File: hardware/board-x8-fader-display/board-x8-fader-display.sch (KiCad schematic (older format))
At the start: 10 parts

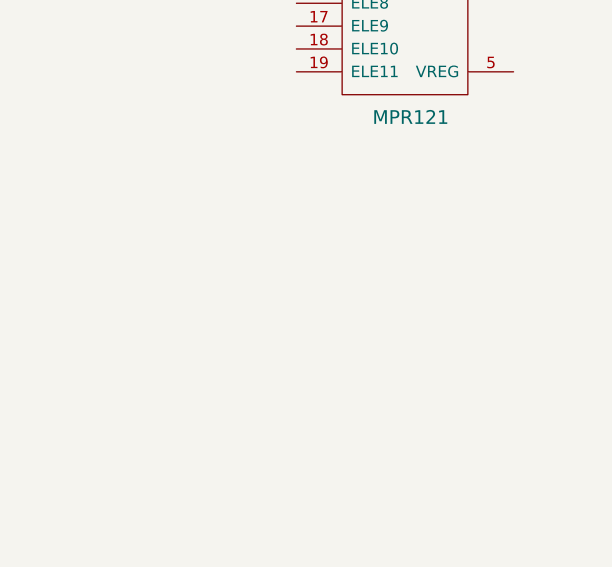
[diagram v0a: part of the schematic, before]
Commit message: Adding L293 lib, moving motor to sensible place in fader lib
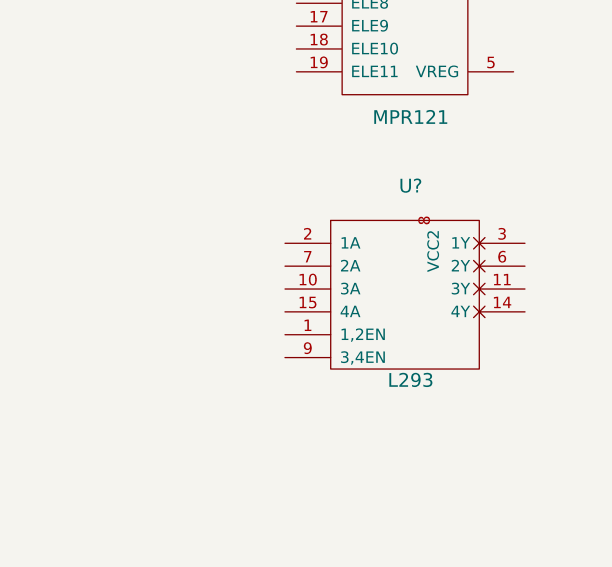
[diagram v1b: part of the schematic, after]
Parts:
- added U?: L293, symbol L293
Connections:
- net GND: now also U?.12 (GND), U?.13 (GND), U?.4 (GND), U?.5 (GND)
- net VCC: now also U?.16 (VCC)
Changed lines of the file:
@@
 LIBS:contrib
 LIBS:valves
+LIBS:board-x8-fader-display-cache
 EELAYER 25 0
 EELAYER END
@@
 	1    0    0    -1
 $EndComp
+$Comp
+L L293 U?
+U 1 1 5A6CD376
+P 3450 4950
+F 0 "U?" H 3450 5400 60  0000 C CNN
+F 1 "L293" H 3450 4550 60  0000 C CNN
+F 2 "" H 3400 4650 60  0001 C CNN
+F 3 "" H 3400 4650 60  0001 C CNN
+	1    3450 4950
+	1    0    0    -1
+$EndComp

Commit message: Fader board schematic updates
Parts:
- removed U?: L293, symbol L293
- added U?: L293, symbol L293
- added U?: 74xx238, symbol 74xx238
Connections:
- net GND: now also U?.12 (GND), U?.13 (GND), U?.4 (GND), U?.5 (GND), U?.8 (GND)
- net VCC: now also U?.16 (VCC), U?.16 (VCC)
- net at RV?.1: now also RV?.1, RV?.1, RV?.1, RV?.1, RV?.1, RV?.1, RV?.1
- net X0: now reaches RV?.2
- net X0: now also U?.13 (X0)
- net at RV?.3: now also RV?.3, RV?.3, RV?.3, RV?.3, RV?.3, RV?.3, RV?.3
- net at RV?.A: now also U?.3 (1Y)
- net at RV?.B: now also U?.6 (2Y)
- net ELE0: now reaches RV?.T (Touch)
- net ELE0: now also U?.8 (ELE0)
- net X1: now reaches RV?.2
- net X1: now also U?.14 (X1)
- net at RV?.A: now also U?.11 (3Y)
- net at RV?.B: now also U?.14 (4Y)
- net ELE1: now reaches RV?.T (Touch)
- net ELE1: now also U?.9 (ELE1)
- net X2: now reaches RV?.2
- net X2: now also U?.15 (X2)
- net ELE2: now reaches RV?.T (Touch)
- net ELE2: now also U?.10 (ELE2)
- net X3: now reaches RV?.2
- net X3: now also U?.12 (X3)
- net ELE3: now reaches RV?.T (Touch)
- net ELE3: now also U?.11 (ELE3)
- net X4: now reaches RV?.2
- net X4: now also U?.1 (X4)
- net ELE4: now reaches RV?.T (Touch)
- net ELE4: now also U?.12 (ELE4)
- net X5: now reaches RV?.2
- net X5: now also U?.5 (X5)
- net ELE5: now reaches RV?.T (Touch)
- net ELE5: now also U?.13 (ELE5)
- net X6: now reaches RV?.2
- net X6: now also U?.2 (X6)
- net ELE6: now reaches RV?.T (Touch)
- net ELE6: now also U?.14 (ELE6)
- net X7: now reaches RV?.2
- net X7: now also U?.4 (X7)
- net ELE7: now reaches RV?.T (Touch)
- net ELE7: now also U?.15 (ELE7)
- new net: U?.1 (1,2EN), U?.15 (Y0)
- new net: U?.10 (3A), U?.2 (1A)
- new net: U?.15 (4A), U?.7 (2A)
- new net: U?.14 (Y1), U?.9 (3,4EN)
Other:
- moved on the sheet: RV?, U?

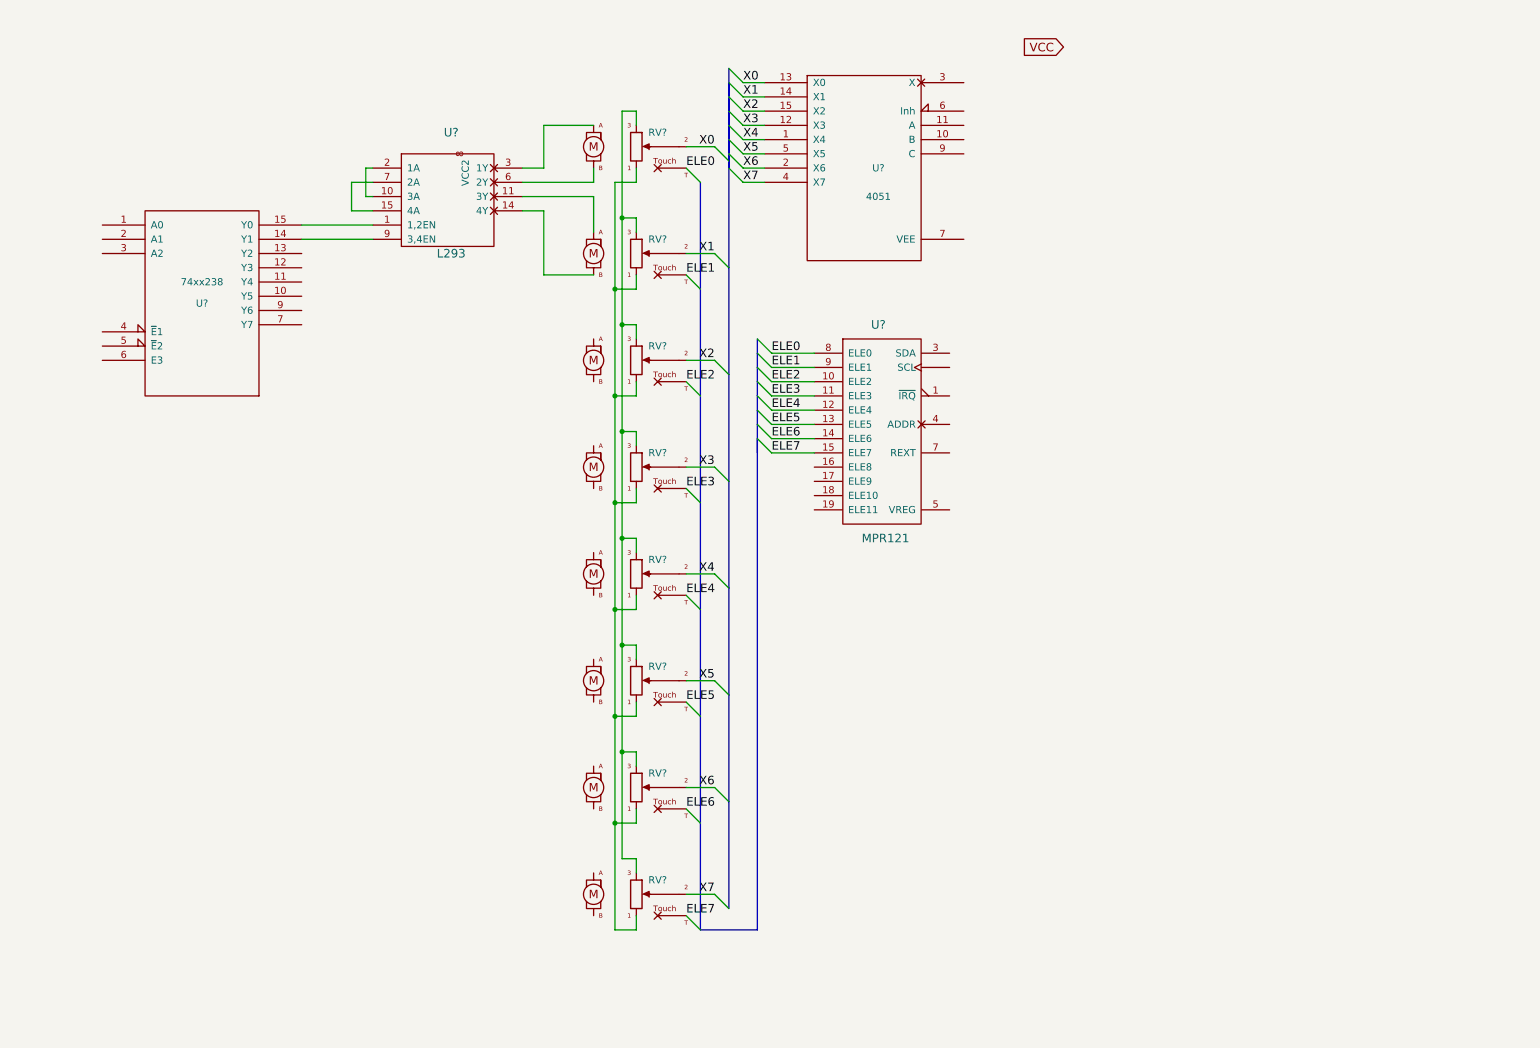
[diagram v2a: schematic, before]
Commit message: adding more wires to schematic, still need board connectors
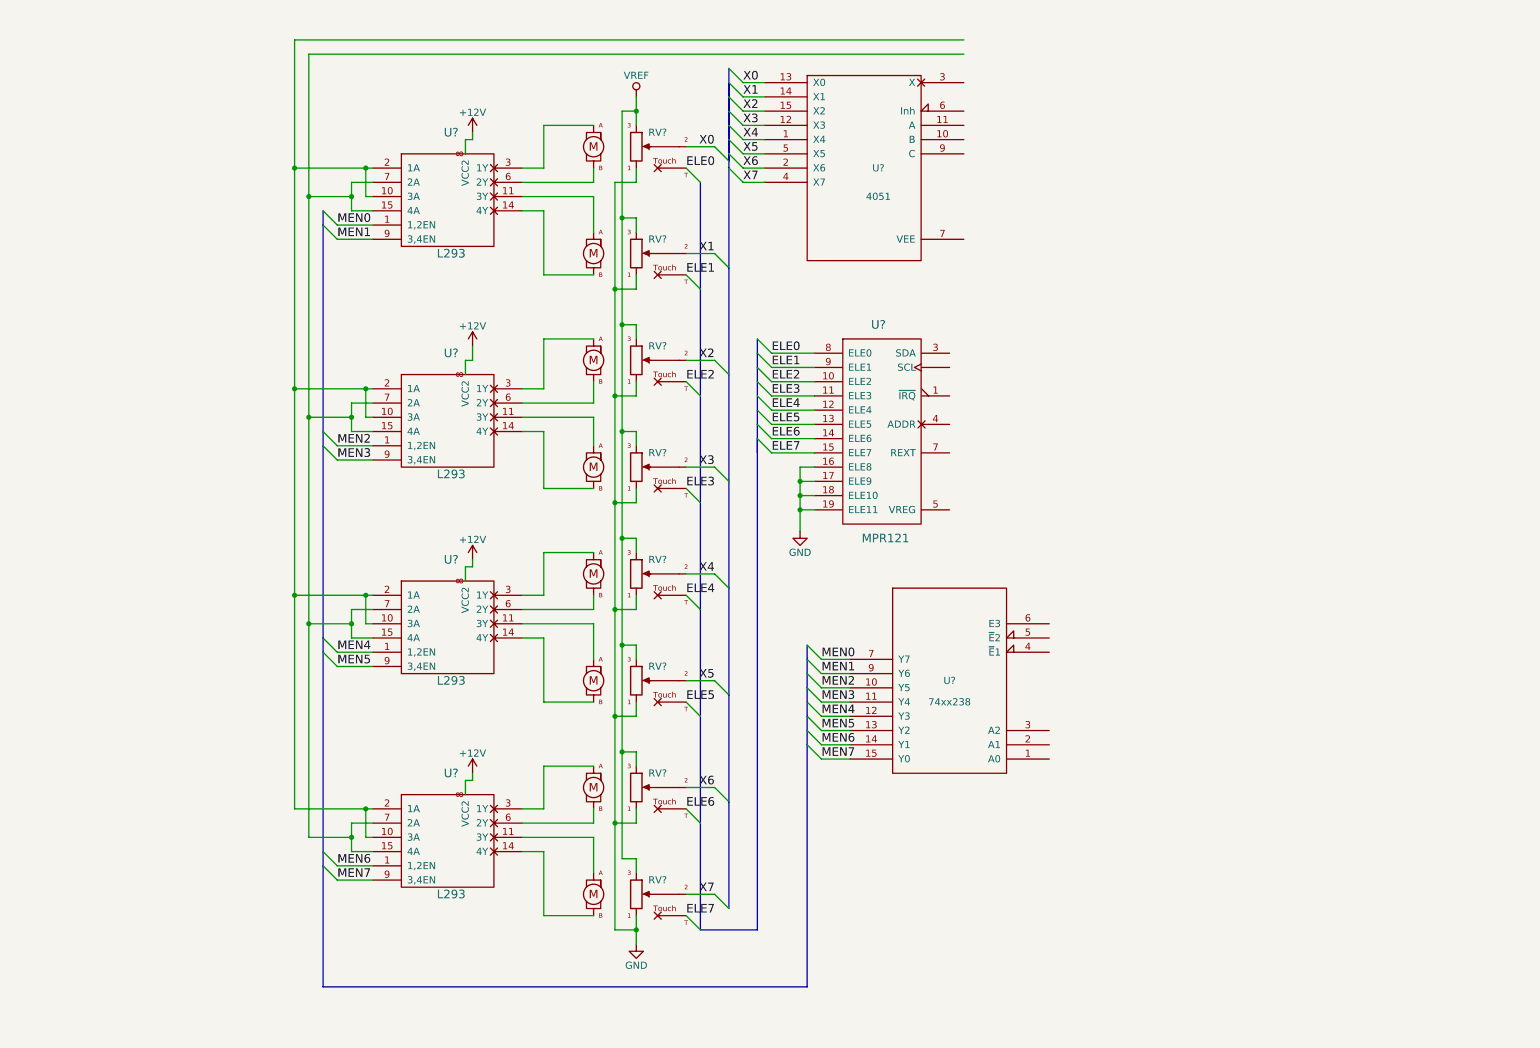
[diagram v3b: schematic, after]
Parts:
- added U? (x3): L293, symbol L293
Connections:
- net GND: now also RV?.3, RV?.3, RV?.3, RV?.3, RV?.3, RV?.3, RV?.3, RV?.3, U?.16 (ELE8), U?.17 (ELE9), U?.18 (ELE10), U?.19 (ELE11), U?.12 (GND), U?.12 (GND), U?.12 (GND), U?.13 (GND), U?.13 (GND), U?.13 (GND), U?.4 (GND), U?.4 (GND), U?.4 (GND), U?.5 (GND), U?.5 (GND), U?.5 (GND)
- net VCC: now also U?.16 (VCC), U?.16 (VCC), U?.16 (VCC)
- net VREF: now reaches RV?.1, RV?.1, RV?.1, RV?.1, RV?.1, RV?.1, RV?.1, RV?.1
- net at RV?.A: now also U?.3 (1Y) (x3)
- net at RV?.B: now also U?.6 (2Y) (x3)
- net at RV?.A: now also U?.11 (3Y) (x3)
- net at RV?.B: now also U?.14 (4Y) (x3)
- net MEN0: now reaches U?.1 (1,2EN)
- net MEN0: now also U?.7 (Y7); no longer U?.15 (Y0)
- net at U?.10 (3A), U?.2 (1A): now also U?.10 (3A), U?.10 (3A), U?.10 (3A), U?.2 (1A), U?.2 (1A), U?.2 (1A)
- net at U?.15 (4A), U?.7 (2A): now also U?.15 (4A), U?.15 (4A), U?.15 (4A), U?.7 (2A), U?.7 (2A), U?.7 (2A)
- net +12V: now reaches U?.8 (VCC2)
- net +12V: now also U?.8 (VCC2), U?.8 (VCC2), U?.8 (VCC2)
- net MEN1: now reaches U?.9 (3,4EN)
- net MEN1: now also U?.9 (Y6); no longer U?.14 (Y1)
- net MEN2: now reaches U?.10 (Y5)
- net MEN2: now also U?.1 (1,2EN)
- net MEN3: now reaches U?.11 (Y4)
- net MEN3: now also U?.9 (3,4EN)
- net MEN4: now reaches U?.12 (Y3)
- net MEN4: now also U?.1 (1,2EN)
- net MEN5: now reaches U?.13 (Y2)
- net MEN5: now also U?.9 (3,4EN)
- new net MEN6: U?.1 (1,2EN), U?.14 (Y1)
- new net MEN7: U?.15 (Y0), U?.9 (3,4EN)
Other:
- moved on the sheet: U?

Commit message: Completed faders and OLED, some bugs with power pins
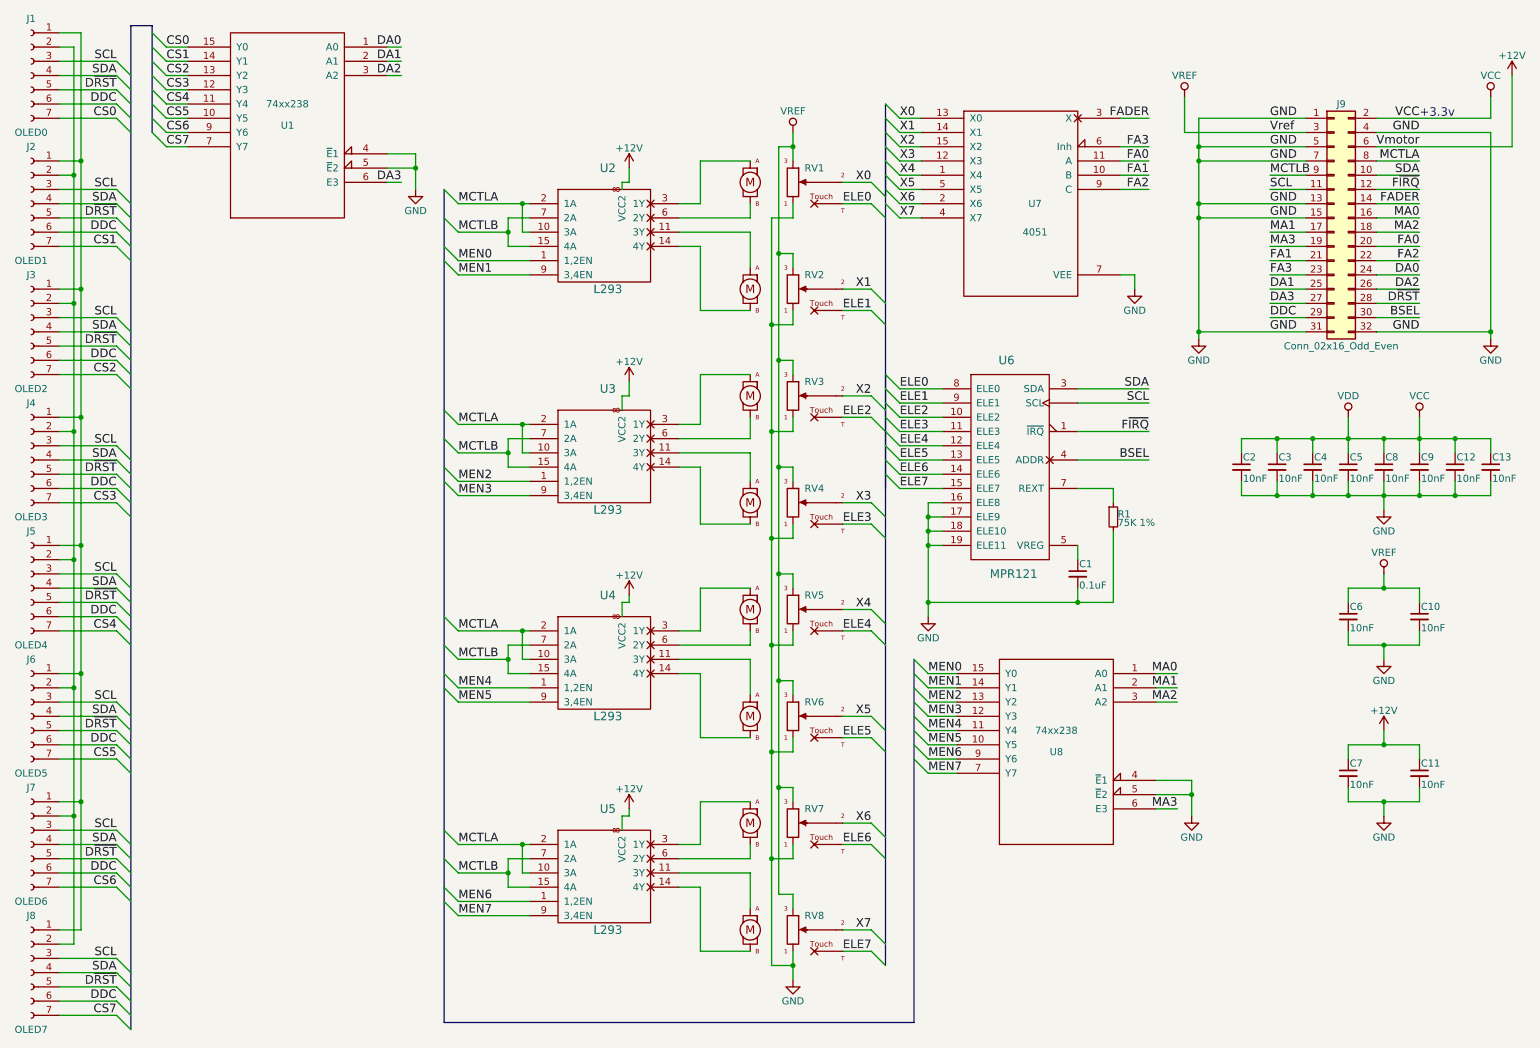
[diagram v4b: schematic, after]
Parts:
- added C1: 0.1uF, symbol C_Small
- added C10, C11, C12, C13, C2, C3, C4, C5, C6, C7, C8, C9: 10nF, symbol C_Small
- added J1: OLED0, symbol Conn_01x07_Female
- added J2: OLED1, symbol Conn_01x07_Female
- added J3: OLED2, symbol Conn_01x07_Female
- added J4: OLED3, symbol Conn_01x07_Female
- added J5: OLED4, symbol Conn_01x07_Female
- added J6: OLED5, symbol Conn_01x07_Female
- added J7: OLED6, symbol Conn_01x07_Female
- added J8: OLED7, symbol Conn_01x07_Female
- added J9: Conn_02x16_Odd_Even, symbol Conn_02x16_Odd_Even
- added R1: 75K 1%, symbol R_Small
- added U1: 74xx238, symbol 74xx238
- gave numbers to parts that had none: 15
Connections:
- net VDD is gone; now on net VCC: U6.20 (VDD)
- net +12V: now also C11.1, C7.1, J9.6 (Pin_6)
- net GND: now also U7.7 (VEE), U8.4 (~E~1), U8.5 (~E~2), C1.2, C10.2, C11.2, C12.2, C13.2, C2.2, C3.2, C4.2, C5.2, C6.2, C7.2, C8.2, C9.2, J9.1 (Pin_1), J9.13 (Pin_13), J9.15 (Pin_15), J9.31 (Pin_31), J9.32 (Pin_32), J9.4 (Pin_4), J9.5 (Pin_5), J9.7 (Pin_7), R1.2, U1.4 (~E~1), U1.5 (~E~2), U1.8 (GND)
- net MEN0: now also U8.15 (Y0); no longer U8.7 (Y7)
- net MEN1: now also U8.14 (Y1); no longer U8.9 (Y6)
- net MEN2: now also U8.13 (Y2); no longer U8.10 (Y5)
- net MEN3: now also U8.12 (Y3); no longer U8.11 (Y4)
- net MEN4: now also U8.11 (Y4); no longer U8.12 (Y3)
- net MEN5: now also U8.10 (Y5); no longer U8.13 (Y2)
- net MEN6: now also U8.9 (Y6); no longer U8.14 (Y1)
- net MEN7: now also U8.7 (Y7); no longer U8.15 (Y0)
- net VCC: now also C12.1, C13.1, C2.1, C3.1, C4.1, C5.1, C8.1, C9.1, J9.2 (Pin_2), U1.16 (VCC)
- net VREF: now also C10.1, C6.1, J9.3 (Pin_3)
- net F~IRQ~: now reaches U6.1 (~IRQ~)
- net F~IRQ~: now also J9.12 (Pin_12)
- net SDA: now reaches U6.3 (SDA)
- net SDA: now also J1.4 (Pin_4), J2.4 (Pin_4), J3.4 (Pin_4), J4.4 (Pin_4), J5.4 (Pin_4), J6.4 (Pin_4), J7.4 (Pin_4), J8.4 (Pin_4), J9.10 (Pin_10)
- net BSEL: now reaches U6.4 (ADDR)
- net BSEL: now also J9.30 (Pin_30)
- net at U6.5 (VREG): now also C1.1
- net at U6.7 (REXT): now also R1.1
- net SCL: now reaches U6.~ (SCL)
- net SCL: now also J1.3 (Pin_3), J2.3 (Pin_3), J3.3 (Pin_3), J4.3 (Pin_3), J5.3 (Pin_3), J6.3 (Pin_3), J7.3 (Pin_3), J8.3 (Pin_3), J9.11 (Pin_11)
- net FA1: now reaches U7.10 (B)
- net FA1: now also J9.21 (Pin_21)
- net FA0: now reaches U7.11 (A)
- net FA0: now also J9.20 (Pin_20)
- net FADER: now reaches U7.3 (X)
- net FADER: now also J9.14 (Pin_14)
- net FA3: now reaches U7.6 (Inh)
- net FA3: now also J9.23 (Pin_23)
- net FA2: now reaches U7.9 (C)
- net FA2: now also J9.22 (Pin_22)
- net MCTLA: now reaches U2.10 (3A), U2.2 (1A), U3.10 (3A), U3.2 (1A), U4.10 (3A), U4.2 (1A), U5.10 (3A), U5.2 (1A)
- net MCTLA: now also J9.8 (Pin_8)
- net MCTLB: now reaches U2.15 (4A), U2.7 (2A), U3.15 (4A), U3.7 (2A), U4.15 (4A), U4.7 (2A), U5.15 (4A), U5.7 (2A)
- net MCTLB: now also J9.9 (Pin_9)
- net MA0: now reaches U8.1 (A0)
- net MA0: now also J9.16 (Pin_16)
- net MA1: now reaches U8.2 (A1)
- net MA1: now also J9.17 (Pin_17)
- net MA2: now reaches U8.3 (A2)
- net MA2: now also J9.18 (Pin_18)
- net MA3: now reaches U8.6 (E3)
- net MA3: now also J9.19 (Pin_19)
- new net: J1.1 (Pin_1), J2.1 (Pin_1), J3.1 (Pin_1), J4.1 (Pin_1), J5.1 (Pin_1), J6.1 (Pin_1), J7.1 (Pin_1), J8.1 (Pin_1)
- new net: J1.2 (Pin_2), J2.2 (Pin_2), J3.2 (Pin_2), J4.2 (Pin_2), J5.2 (Pin_2), J6.2 (Pin_2), J7.2 (Pin_2), J8.2 (Pin_2)
- new net CS0: J1.7 (Pin_7), U1.15 (Y0)
- new net CS1: J2.7 (Pin_7), U1.14 (Y1)
- new net CS2: J3.7 (Pin_7), U1.13 (Y2)
- new net CS3: J4.7 (Pin_7), U1.12 (Y3)
- new net CS4: J5.7 (Pin_7), U1.11 (Y4)
- new net CS5: J6.7 (Pin_7), U1.10 (Y5)
- new net CS6: J7.7 (Pin_7), U1.9 (Y6)
- new net CS7: J8.7 (Pin_7), U1.7 (Y7)
- new net DA0: J9.24 (Pin_24), U1.1 (A0)
- new net DA1: J9.25 (Pin_25), U1.2 (A1)
- new net DA2: J9.26 (Pin_26), U1.3 (A2)
- new net DA3: J9.27 (Pin_27), U1.6 (E3)
- new net DDC: J1.6 (Pin_6), J2.6 (Pin_6), J3.6 (Pin_6), J4.6 (Pin_6), J5.6 (Pin_6), J6.6 (Pin_6), J7.6 (Pin_6), J8.6 (Pin_6), J9.29 (Pin_29)
- new net D~RST~: J1.5 (Pin_5), J2.5 (Pin_5), J3.5 (Pin_5), J4.5 (Pin_5), J5.5 (Pin_5), J6.5 (Pin_5), J7.5 (Pin_5), J8.5 (Pin_5), J9.28 (Pin_28)
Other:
- note added: "+3.3v"
- moved on the sheet: RV1, RV2, RV3, RV4, RV5, RV6, RV7, RV8, U2, U3, U4, U5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
